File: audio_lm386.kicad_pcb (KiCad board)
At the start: 2 copper layers, 33.5 x 19.1 mm, 14 parts, among them J1 Screw_Terminal_01x02, J2 Screw_Terminal_01x02, J3 ST-025, U1 LM386

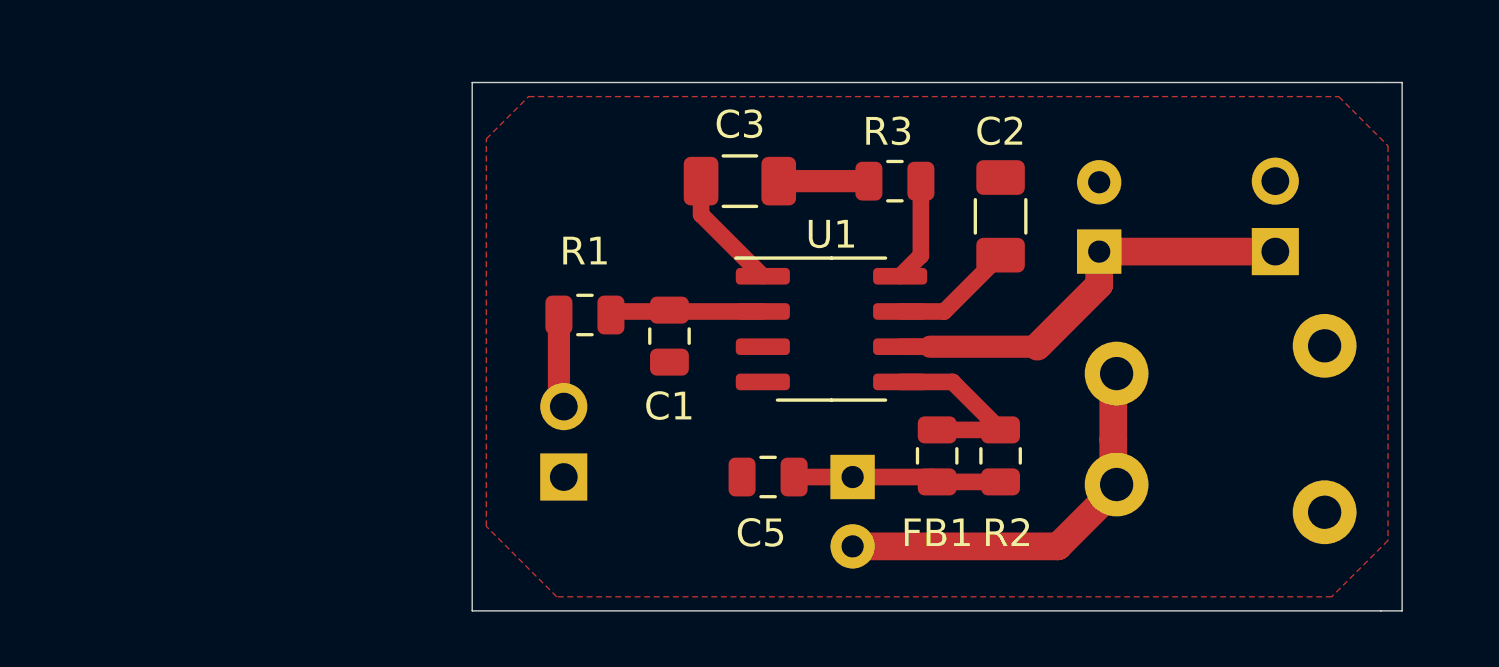
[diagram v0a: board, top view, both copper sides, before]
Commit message: добавлен предусилитель с пинами для подключения потенциометра
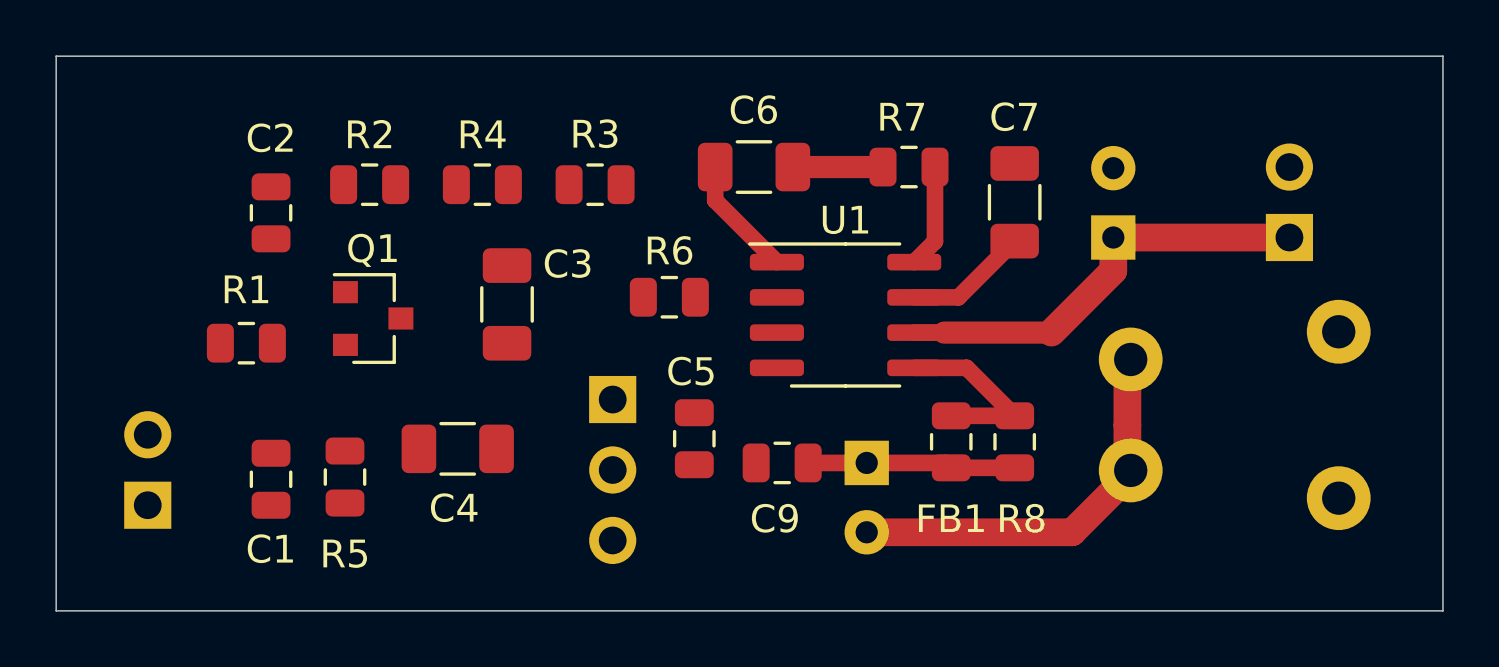
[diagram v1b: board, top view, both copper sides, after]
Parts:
- added C10: 220uF, Capacitor_THT:CP_Radial_D6.3mm_P2.50mm, B.Cu at (118.6, 70.9)
- added C7: 10uF, Capacitor_SMD:C_1206_3216Metric, F.Cu at (124.0, 61.5)
- added C8: 220uF, Capacitor_THT:CP_Radial_D5.0mm_P2.50mm, B.Cu at (127.5, 62.7)
- added C9: 47n, Capacitor_SMD:C_0805_2012Metric, F.Cu at (115.6, 70.9)
- added J4: ST-025, AM_Radio:ST-025 audio_jack, B.Cu at (135.6, 72.1)
- added Q1: MMBT5551L, Package_TO_SOT_SMD:SOT-23, F.Cu at (100.8, 65.7)
- added R4: 10k, Resistor_SMD:R_0805_2012Metric, F.Cu at (104.8, 60.8)
- added R5: 10k, Resistor_SMD:R_0805_2012Metric, F.Cu at (99.8, 71.4)
- added R6: 10k, Resistor_SMD:R_0805_2012Metric, F.Cu at (111.5, 64.9)
- added R7: 1k, Resistor_SMD:R_0805_2012Metric, F.Cu at (120.1, 60.2)
- added R8: 47, Resistor_SMD:R_0805_2012Metric, F.Cu at (124.0, 70.1)
- C2: value 10uF -> 47n; footprint Capacitor_SMD:C_1206_3216Metric -> Capacitor_SMD:C_0805_2012Metric
- C4: value 220uF -> 10uF; footprint Capacitor_THT:CP_Radial_D5.0mm_P2.50mm -> Capacitor_SMD:C_1206_3216Metric; moved to F.Cu
- C5: value 47n -> 2n2
- C6: value 220uF -> 10uF; footprint Capacitor_THT:CP_Radial_D6.3mm_P2.50mm -> Capacitor_SMD:C_1206_3216Metric; moved to F.Cu
- J2: value Screw_Terminal_01x02 -> Screw_Terminal_01x03; footprint Connector_PinHeader_2.54mm:PinHeader_1x02_P2.54mm_Vertical -> Connector_PinHeader_2.54mm:PinHeader_1x03_P2.54mm_Vertical
- J3: value ST-025 -> Screw_Terminal_01x02; footprint AM_Radio:ST-025 audio_jack -> Connector_PinHeader_2.54mm:PinHeader_1x02_P2.54mm_Vertical
- R2: value 47 -> 10k
- R3: value 1k -> 10k
- moved C2 26.3 mm to (97.1, 61.8), turned to 270 degrees
- moved R2 24.8 mm to (100.7, 60.8), turned to 0 degrees
- moved J2 24.5 mm to (109.5, 68.6), turned to 180 degrees
- moved C4 24.2 mm to (103.9, 70.4), turned to 0 degrees
- moved C1 15.3 mm to (97.1, 71.5)
- moved J1 15.0 mm to (92.7, 72.4)
- moved R1 12.2 mm to (96.3, 66.5)
- moved C6 11.7 mm to (114.6, 60.2), turned to 0 degrees
- moved R3 10.8 mm to (108.8, 60.8)
- moved J3 9.99 mm to (133.9, 62.7), turned to 0 degrees
- moved C3 9.50 mm to (105.7, 65.2), turned to 270 degrees
- moved C5 3.00 mm to (112.4, 70.0), turned to 270 degrees
- moved U1 0.72 mm to (117.9, 65.5)
- moved FB1 0.72 mm to (121.7, 70.1)
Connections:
- C2 pad 2: GND -> Net-(C1-Pad1)
- C3 pad 2: Net-(C3-Pad2) -> GND
- C4 pad 2: GND -> Net-(C4-Pad2)
- C6 pad 1: Net-(C5-Pad1) -> Net-(C6-Pad1)
- FB1 pad 1: Net-(C5-Pad1) -> Net-(C10-Pad1)
- J2 pad 1: Net-(C4-Pad1) -> Net-(C4-Pad2)
- J2 pad 2: GND -> Net-(J2-Pad2)
- R2 pad 1: Net-(C5-Pad1) -> Net-(C2-Pad1)
- R2 pad 2: Net-(FB1-Pad2) -> Net-(C4-Pad1)
- R3 pad 1: Net-(C3-Pad2) -> Net-(C3-Pad1)
- R3 pad 2: Net-(R3-Pad2) -> Net-(C8-Pad1)
- U1 pad 1: Net-(C3-Pad1) -> Net-(C6-Pad1)
- U1 pad 2: Net-(C1-Pad1) -> Net-(C5-Pad1)
- U1 pad 6: Net-(C4-Pad1) -> Net-(C8-Pad1)
- U1 pad 7: Net-(C2-Pad1) -> Net-(C7-Pad1)
- U1 pad 8: Net-(R3-Pad2) -> Net-(R7-Pad2)
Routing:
- net Net-(C8-Pad1): track 0.00 -> 15.7 mm
- net Net-(C4-Pad1): track 15.7 -> 0.00 mm
- net Net-(C10-Pad2): track 0.00 -> 13.8 mm
- net Net-(C6-Pad2): track 13.8 -> 3.25 mm
- net Net-(C5-Pad1): track 7.52 -> 0.00 mm
- net Net-(C10-Pad1): track 0.00 -> 7.52 mm
- net Net-(C1-Pad1): track 5.53 -> 0.00 mm
- net Net-(C2-Pad1): track 4.46 -> 0.00 mm
- net Net-(C7-Pad1): track 0.00 -> 4.46 mm
- net Net-(C3-Pad1): track 4.44 -> 0.00 mm
- net Net-(C6-Pad1): track 0.00 -> 4.44 mm
- net Net-(R3-Pad2): track 3.74 -> 0.00 mm
- net Net-(R7-Pad2): track 0.00 -> 3.74 mm
- net Net-(J1-Pad2): track 3.37 -> 0.00 mm
- net Net-(C3-Pad2): track 3.25 -> 0.00 mm
- removed copper zone on F.Cu, net GND
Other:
- board size 33.5 x 19.1 mm -> 50 x 20 mm

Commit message: выполнена трассировка для предусилителя с пинами для подключения потенциометра
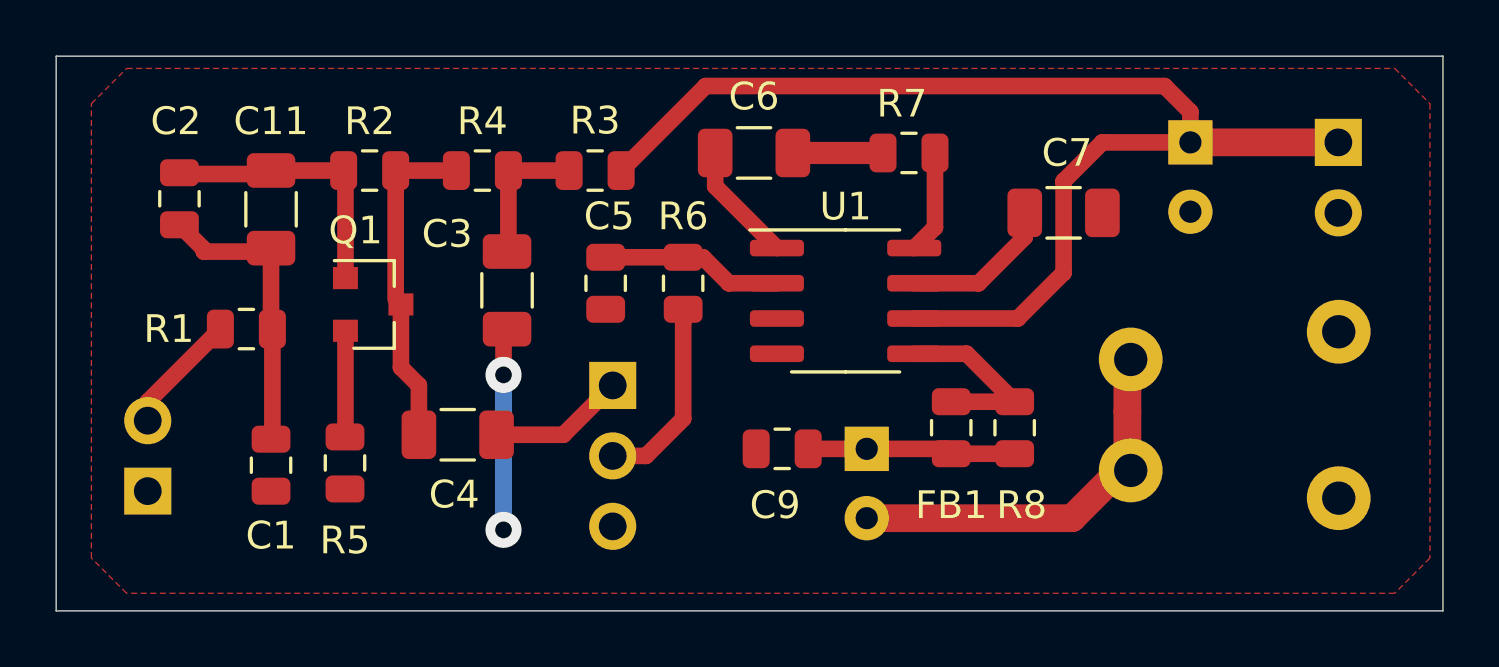
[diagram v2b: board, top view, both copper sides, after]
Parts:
- added C11: 10uF, Capacitor_SMD:C_1206_3216Metric, F.Cu at (97.1, 61.7)
- R2: value 10k -> 330k
- R3: value 10k -> 100
- R4: value 10k -> 3k3
- R5: value 10k -> 120
- moved C5 6.45 mm to (109.2, 64.4)
- moved C8 4.41 mm to (130.3, 59.3), turned to 270 degrees
- moved J3 3.86 mm to (135.6, 59.3), turned to 180 degrees
- moved C2 3.34 mm to (93.8, 61.3)
- moved C7 1.80 mm to (125.7, 61.8), turned to 0 degrees
- moved R6 0.71 mm to (112.0, 64.4), turned to 90 degrees
- moved C4 0.51 mm to (103.9, 69.8)
- moved Q1 0.51 mm to (100.8, 65.2)
- moved C6 0.51 mm to (114.6, 59.7)
- moved R7 0.51 mm to (120.1, 59.7)
- moved C1 0.51 mm to (97.1, 70.9)
- moved C10 0.51 mm to (118.6, 70.4)
- moved C3 0.51 mm to (105.7, 64.6)
- moved C9 0.51 mm to (115.6, 70.4)
- moved FB1 0.51 mm to (121.7, 69.6)
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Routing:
- net Net-(C8-Pad1): track 15.7 -> 44.2 mm
- net Net-(C4-Pad1): track 0.00 -> 12.1 mm
- net Net-(C1-Pad1): track 0.00 -> 10.6 mm
- net Net-(C11-Pad1): track 0.00 -> 9.87 mm
- net GND: track 0.00 -> 7.29 mm, vias 0 -> 2
- net Net-(J2-Pad2): track 0.00 -> 7.04 mm
- net Net-(C5-Pad1): track 0.00 -> 6.57 mm
- net Net-(C3-Pad1): track 0.00 -> 5.13 mm
- net Net-(C4-Pad2): track 0.00 -> 4.92 mm
- net Net-(J1-Pad2): track 0.00 -> 4.39 mm
- net Net-(Q1-Pad2): track 0.00 -> 3.83 mm
- net Net-(C7-Pad1): track 4.46 -> 5.55 mm
- added copper zone on F.Cu, net GND
